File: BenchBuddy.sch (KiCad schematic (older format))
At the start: 0 parts

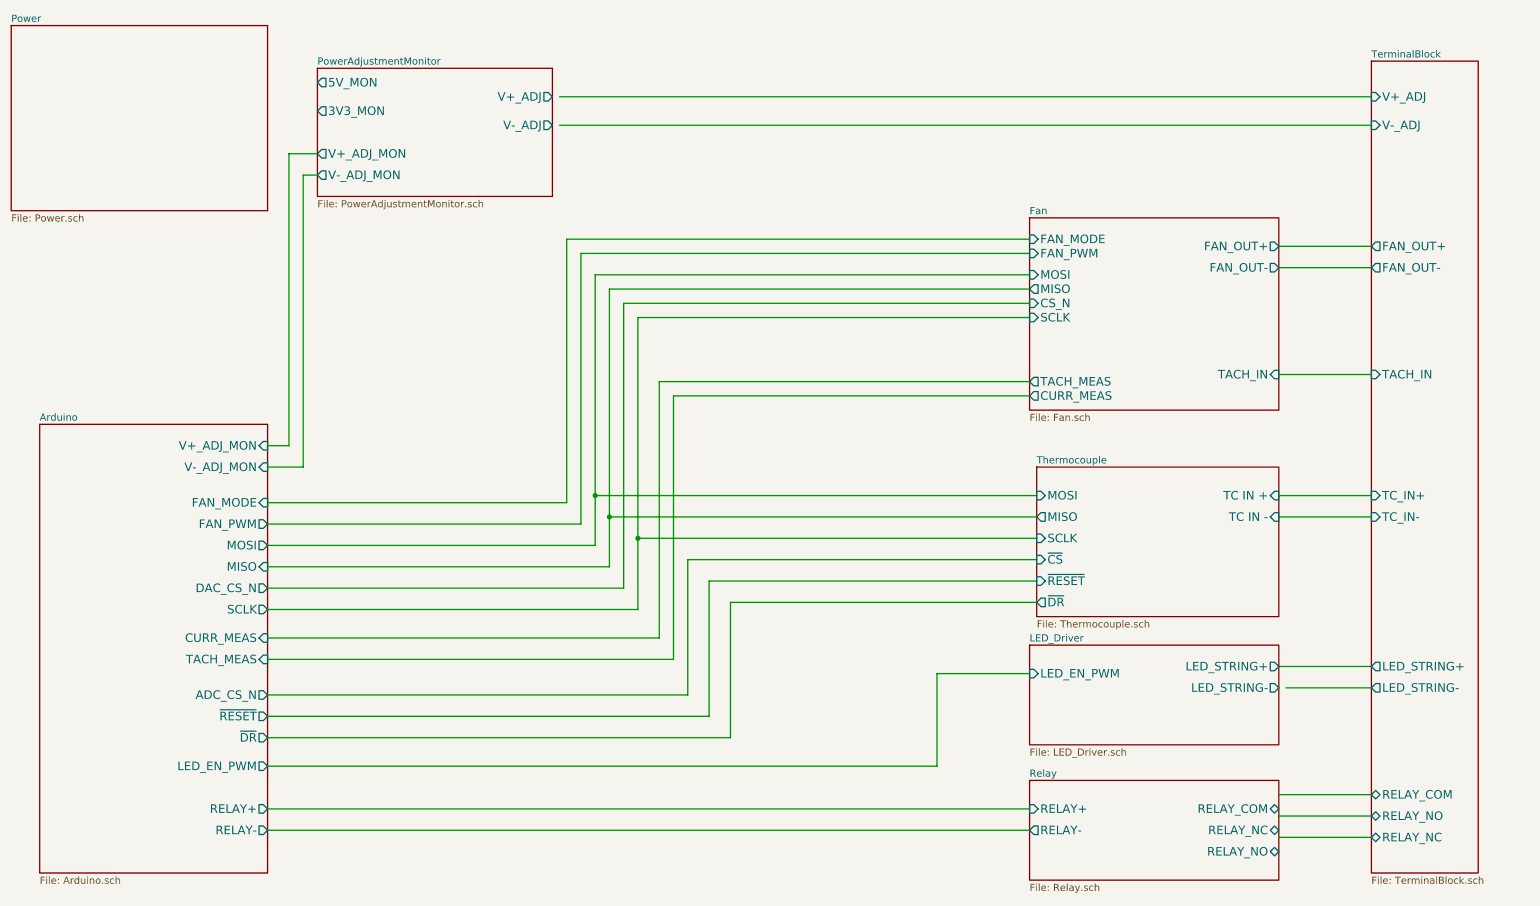
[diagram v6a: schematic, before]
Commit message: Associating Current Module
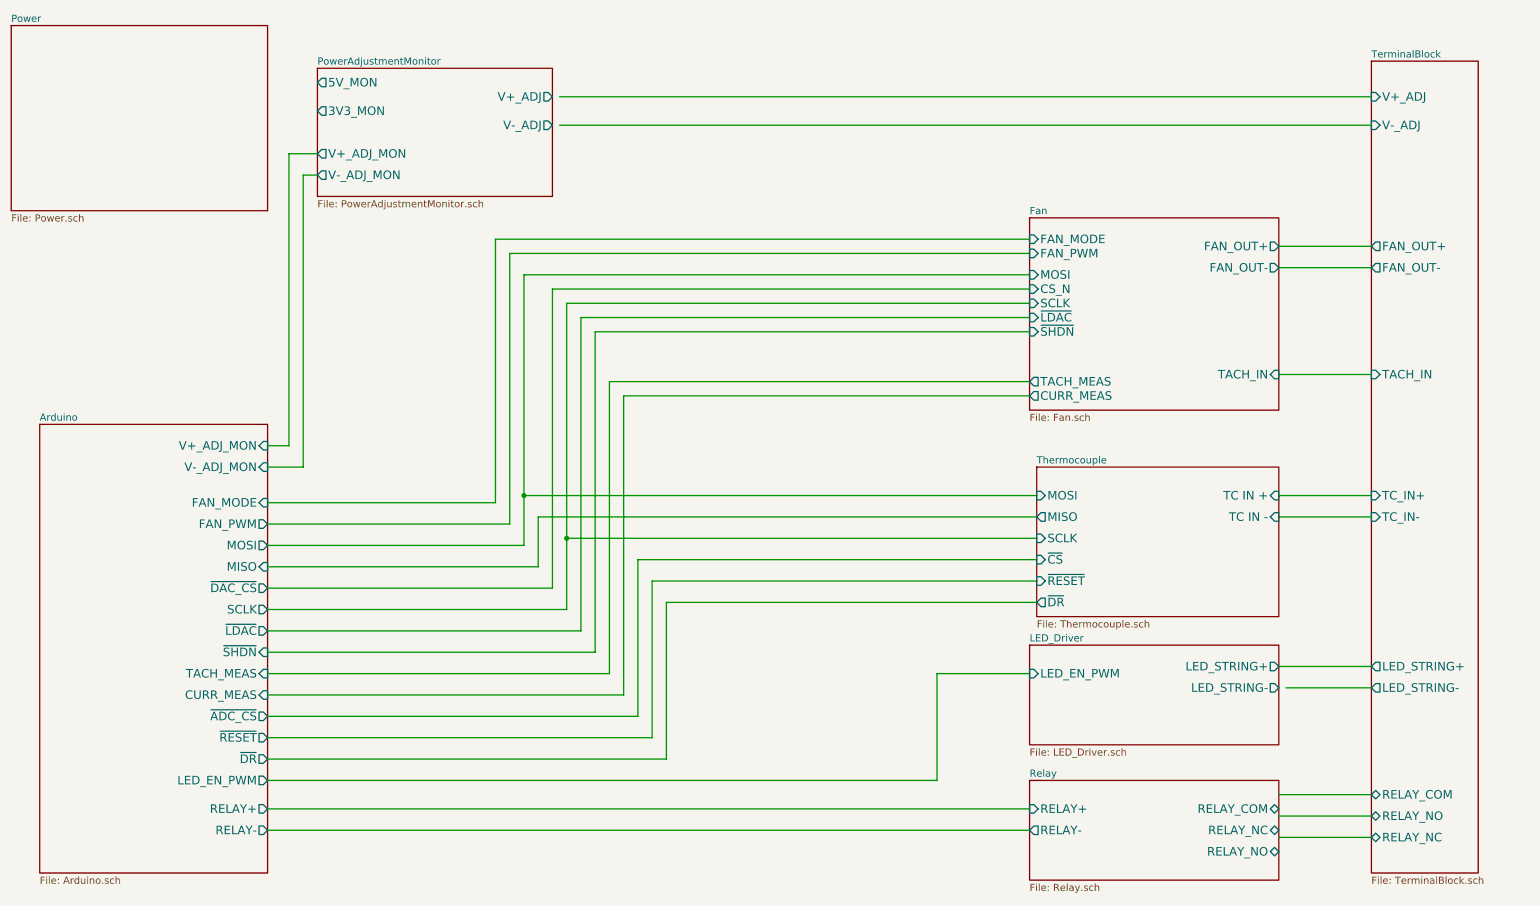
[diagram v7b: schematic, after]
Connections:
- wire segments 59 -> 64
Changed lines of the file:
@@
-EESchema Schematic File Version 2  date 10/13/2013 2:17:45 PM
+EESchema Schematic File Version 2  date 10/13/2013 8:19:10 PM
 LIBS:power
 LIBS:device
@@
 Sheet 1 9
 Title "noname.sch"
-Date "13 oct 2013"
+Date "14 oct 2013"
 Rev ""
 Comp ""
@@
 	2650 1650 2750 1650
 Wire Wire Line
-	2400 4100 4600 4100
-Wire Wire Line
-	4600 4100 4600 2200
-Wire Wire Line
-	4600 2200 7750 2200
-Wire Wire Line
-	7750 2350 4700 2350
-Wire Wire Line
-	4700 2350 4700 4250
-Wire Wire Line
-	4700 4250 2400 4250
-Wire Wire Line
-	7750 2450 4800 2450
-Wire Wire Line
-	4800 2450 4800 4400
-Wire Wire Line
-	4800 4400 2400 4400
-Wire Wire Line
-	7750 2550 4900 2550
-Wire Wire Line
-	4900 2550 4900 4550
-Wire Wire Line
-	5000 2650 5000 4700
-Wire Wire Line
-	5000 4700 2400 4700
-Wire Wire Line
-	7750 3100 5150 3100
-Wire Wire Line
-	5150 3100 5150 4900
-Wire Wire Line
-	5150 4900 2400 4900
-Wire Wire Line
-	7750 3200 5250 3200
-Wire Wire Line
-	5250 3200 5250 5050
-Wire Wire Line
-	5250 5050 2400 5050
-Wire Wire Line
-	7800 3900 4700 3900
-Connection ~ 4700 3900
-Wire Wire Line
-	7800 4050 4800 4050
-Connection ~ 4800 4050
-Wire Wire Line
-	4900 4550 2400 4550
-Wire Wire Line
-	7800 4350 5350 4350
-Wire Wire Line
-	5350 4350 5350 5300
-Wire Wire Line
-	5350 5300 2400 5300
-Wire Wire Line
-	2400 5800 7100 5800
-Wire Wire Line
-	7100 5800 7100 5150
+	2400 4100 4100 4100
+Wire Wire Line
+	4100 4100 4100 2200
+Wire Wire Line
+	4100 2200 7750 2200
+Wire Wire Line
+	7750 2350 4200 2350
+Wire Wire Line
+	4200 2350 4200 4250
+Wire Wire Line
+	4200 4250 2400 4250
+Wire Wire Line
+	4300 4400 2400 4400
+Wire Wire Line
+	4400 2450 4400 4550
+Wire Wire Line
+	4500 2550 4500 4700
+Wire Wire Line
+	4500 4700 2400 4700
+Wire Wire Line
+	4800 3100 7750 3100
+Wire Wire Line
+	4900 3200 7750 3200
+Wire Wire Line
+	4200 3900 7800 3900
+Connection ~ 4200 3900
+Wire Wire Line
+	7800 4050 4300 4050
+Wire Wire Line
+	4400 4550 2400 4550
+Wire Wire Line
+	5000 4350 7800 4350
+Wire Wire Line
+	7100 5150 7100 5900
 Wire Wire Line
 	7100 5150 7750 5150
@@
 	10150 4050 9500 4050
 Wire Wire Line
-	7750 2650 5000 2650
-Wire Wire Line
-	7800 4200 5000 4200
-Connection ~ 5000 4200
-$Sheet
-S 800  3400 1600 3150
-U 522FEA6C
-F0 "Arduino" 50
-F1 "Arduino.sch" 50
-F2 "MOSI" O R 2400 4250 60
-F3 "MISO" I R 2400 4400 60
-F4 "SCLK" O R 2400 4700 60
-F5 "TACH_MEAS" I R 2400 5050 60
-F6 "RELAY+" O R 2400 6100 60
-F7 "RELAY-" O R 2400 6250 60
-F8 "CURR_MEAS" I R 2400 4900 60
-F9 "V+_ADJ_MON" I R 2400 3550 60
-F10 "V-_ADJ_MON" I R 2400 3700 60
-F11 "LED_EN_PWM" O R 2400 5800 60
-F12 "DAC_CS_N" O R 2400 4550 60
-F13 "ADC_CS_N" O R 2400 5300 60
-F14 "FAN_PWM" O R 2400 4100 60
-F15 "FAN_MODE" I R 2400 3950 60
-F16 "~RESET" O R 2400 5450 60
-F17 "~DR" O R 2400 5600 60
-$EndSheet
-Wire Wire Line
-	7750 2100 4500 2100
-Wire Wire Line
-	4500 2100 4500 3950
-Wire Wire Line
-	4500 3950 2400 3950
+	7800 4200 4500 4200
+Connection ~ 4500 4200
+Wire Wire Line
+	7750 2100 4000 2100
+Wire Wire Line
+	4000 2100 4000 3950
+Wire Wire Line
+	4000 3950 2400 3950
 $Sheet
 S 7750 1950 1750 1350
@@
 F1 "Fan.sch" 50
 F2 "MOSI" I L 7750 2350 60
-F3 "MISO" O L 7750 2450 60
-F4 "CS_N" I L 7750 2550 60
-F5 "SCLK" I L 7750 2650 60
-F6 "FAN_OUT+" O R 9500 2150 60
-F7 "TACH_IN" I R 9500 3050 60
-F8 "TACH_MEAS" O L 7750 3100 60
-F9 "CURR_MEAS" O L 7750 3200 60
-F10 "FAN_OUT-" O R 9500 2300 60
-F11 "FAN_PWM" I L 7750 2200 60
-F12 "FAN_MODE" I L 7750 2100 60
+F3 "CS_N" I L 7750 2450 60
+F4 "SCLK" I L 7750 2550 60
+F5 "FAN_OUT+" O R 9500 2150 60
+F6 "TACH_IN" I R 9500 3050 60
+F7 "TACH_MEAS" O L 7750 3100 60
+F8 "CURR_MEAS" O L 7750 3200 60
+F9 "FAN_OUT-" O R 9500 2300 60
+F10 "FAN_PWM" I L 7750 2200 60
+F11 "FAN_MODE" I L 7750 2100 60
+F12 "~LDAC" I L 7750 2650 60
+F13 "~SHDN" I L 7750 2750 60
 $EndSheet
 $Sheet
@@
 	9550 5250 10150 5250
 Wire Wire Line
-	2400 5450 5500 5450
-Wire Wire Line
-	5500 5450 5500 4500
-Wire Wire Line
-	5500 4500 7800 4500
-Wire Wire Line
-	7800 4650 5650 4650
-Wire Wire Line
-	5650 4650 5650 5600
-Wire Wire Line
-	5650 5600 2400 5600
+	5100 4500 7800 4500
+Wire Wire Line
+	5200 4650 7800 4650
+Wire Wire Line
+	4300 4050 4300 4400
+Wire Wire Line
+	4500 2550 7750 2550
+Wire Wire Line
+	4400 2450 7750 2450
+Wire Wire Line
+	2400 4850 4600 4850
+Wire Wire Line
+	4600 4850 4600 2650
+Wire Wire Line
+	4600 2650 7750 2650
+Wire Wire Line
+	7750 2750 4700 2750
+Wire Wire Line
+	4700 2750 4700 5000
+Wire Wire Line
+	4700 5000 2400 5000
+$Sheet
+S 800  3400 1600 3150
+U 522FEA6C
+F0 "Arduino" 50
+F1 "Arduino.sch" 50
+F2 "MOSI" O R 2400 4250 60
+F3 "MISO" I R 2400 4400 60
+F4 "SCLK" O R 2400 4700 60
+F5 "TACH_MEAS" I R 2400 5150 60
+F6 "RELAY+" O R 2400 6100 60
+F7 "RELAY-" O R 2400 6250 60
+F8 "CURR_MEAS" I R 2400 5300 60
+F9 "V+_ADJ_MON" I R 2400 3550 60
+F10 "V-_ADJ_MON" I R 2400 3700 60
+F11 "LED_EN_PWM" O R 2400 5900 60
+F12 "FAN_PWM" O R 2400 4100 60
+F13 "FAN_MODE" I R 2400 3950 60
+F14 "~RESET" O R 2400 5600 60
+F15 "~DR" O R 2400 5750 60
+F16 "~LDAC" O R 2400 4850 60
+F17 "~SHDN" I R 2400 5000 60
+F18 "~DAC_CS" O R 2400 4550 60
+F19 "~ADC_CS" O R 2400 5450 60
+$EndSheet
+Wire Wire Line
+	2400 5150 4800 5150
+Wire Wire Line
+	4800 5150 4800 3100
+Wire Wire Line
+	4900 3200 4900 5300
+Wire Wire Line
+	4900 5300 2400 5300
+Wire Wire Line
+	2400 5450 5000 5450
+Wire Wire Line
+	5000 5450 5000 4350
+Wire Wire Line
+	5100 4500 5100 5600
+Wire Wire Line
+	5100 5600 2400 5600
+Wire Wire Line
+	2400 5750 5200 5750
+Wire Wire Line
+	5200 5750 5200 4650
+Wire Wire Line
+	7100 5900 2400 5900
 $EndSCHEMATC
